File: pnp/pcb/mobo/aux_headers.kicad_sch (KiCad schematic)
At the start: 0 parts

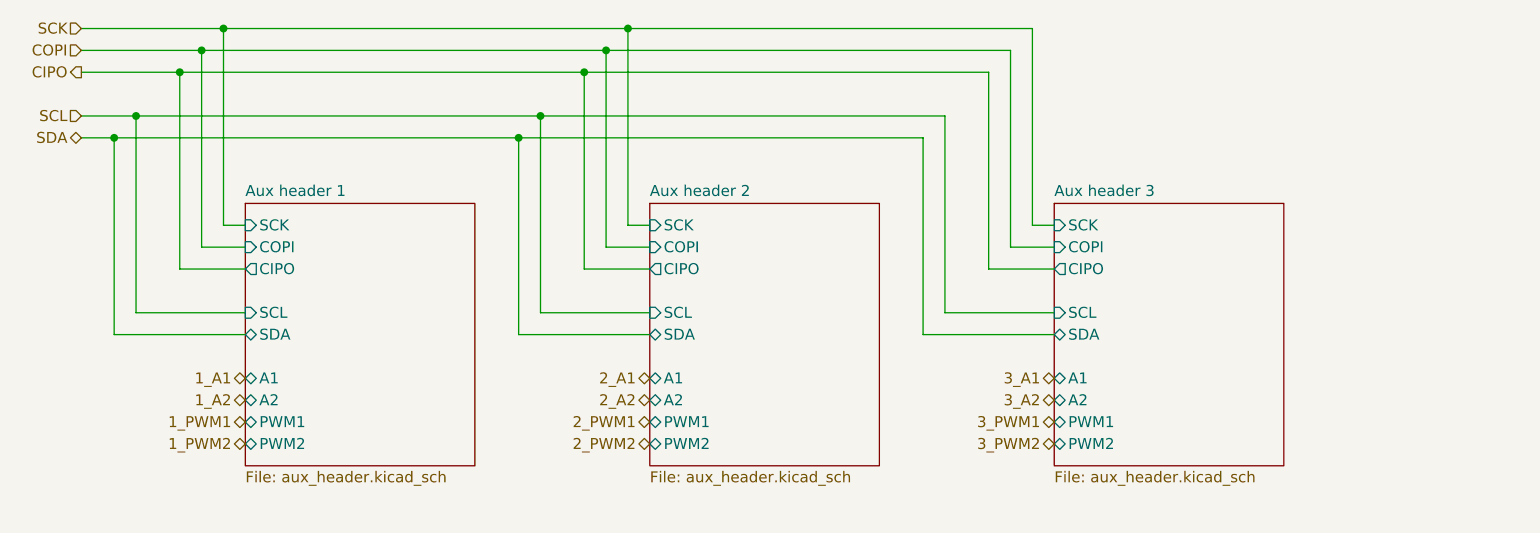
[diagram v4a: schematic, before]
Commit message: adds tons of TVS and inline resistors
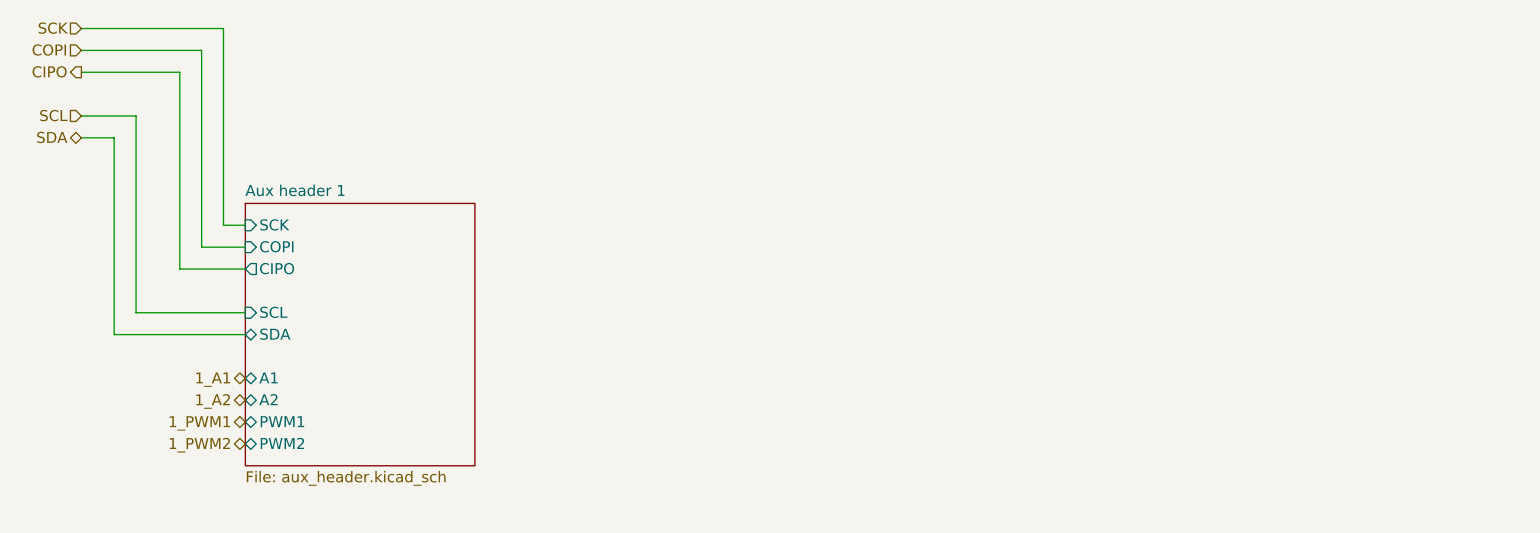
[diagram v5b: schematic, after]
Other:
- removed sheet Aux header 2
- removed sheet Aux header 3
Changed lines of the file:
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@@
     (company "Opulo")
-  )
-  (junction (at 85.09 73.66) (diameter 0) (color 0 0 0 0)
-  )
-  (junction (at 137.16 68.58) (diameter 0) (color 0 0 0 0)
-  )
-  (junction (at 77.47 81.28) (diameter 0) (color 0 0 0 0)
-  )
-  (junction (at 124.46 81.28) (diameter 0) (color 0 0 0 0)
-  )
-  (junction (at 80.01 78.74) (diameter 0) (color 0 0 0 0)
-  )
-  (junction (at 87.63 71.12) (diameter 0) (color 0 0 0 0)
-  )
-  (junction (at 132.08 73.66) (diameter 0) (color 0 0 0 0)
-  )
-  (junction (at 134.62 71.12) (diameter 0) (color 0 0 0 0)
-  )
-  (junction (at 127 78.74) (diameter 0) (color 0 0 0 0)
-  )
-  (junction (at 90.17 68.58) (diameter 0) (color 0 0 0 0)
   )
   (wire (pts (xy 90.17 91.44) (xy 90.17 68.58))
@@
     (stroke (width 0) (type default))
   )
-  (wire (pts (xy 134.62 71.12) (xy 181.61 71.12))
-    (stroke (width 0) (type default))
-  )
   (wire (pts (xy 90.17 91.44) (xy 92.71 91.44))
     (stroke (width 0) (type default))
@@
     (stroke (width 0) (type default))
   )
-  (wire (pts (xy 139.7 101.6) (xy 127 101.6))
-    (stroke (width 0) (type default))
-  )
-  (wire (pts (xy 171.45 104.14) (xy 186.69 104.14))
-    (stroke (width 0) (type default))
-  )
-  (wire (pts (xy 137.16 91.44) (xy 137.16 68.58))
-    (stroke (width 0) (type default))
-  )
-  (wire (pts (xy 127 78.74) (xy 173.99 78.74))
-    (stroke (width 0) (type default))
-  )
-  (wire (pts (xy 179.07 96.52) (xy 186.69 96.52))
-    (stroke (width 0) (type default))
-  )
-  (wire (pts (xy 124.46 81.28) (xy 124.46 104.14))
-    (stroke (width 0) (type default))
-  )
-  (wire (pts (xy 184.15 91.44) (xy 184.15 68.58))
-    (stroke (width 0) (type default))
-  )
-  (wire (pts (xy 181.61 93.98) (xy 186.69 93.98))
-    (stroke (width 0) (type default))
-  )
   (wire (pts (xy 87.63 71.12) (xy 73.66 71.12))
     (stroke (width 0) (type default))
   )
-  (wire (pts (xy 186.69 101.6) (xy 173.99 101.6))
-    (stroke (width 0) (type default))
-  )
-  (wire (pts (xy 173.99 101.6) (xy 173.99 78.74))
-    (stroke (width 0) (type default))
-  )
   (wire (pts (xy 85.09 96.52) (xy 92.71 96.52))
-    (stroke (width 0) (type default))
-  )
-  (wire (pts (xy 124.46 104.14) (xy 139.7 104.14))
-    (stroke (width 0) (type default))
-  )
-  (wire (pts (xy 132.08 96.52) (xy 132.08 73.66))
-    (stroke (width 0) (type default))
-  )
-  (wire (pts (xy 132.08 73.66) (xy 179.07 73.66))
     (stroke (width 0) (type default))
   )
@@
     (stroke (width 0) (type default))
   )
-  (wire (pts (xy 124.46 81.28) (xy 171.45 81.28))
-    (stroke (width 0) (type default))
-  )
   (wire (pts (xy 87.63 93.98) (xy 92.71 93.98))
     (stroke (width 0) (type default))
@@
     (stroke (width 0) (type default))
   )
-  (wire (pts (xy 184.15 91.44) (xy 186.69 91.44))
-    (stroke (width 0) (type default))
-  )
-  (wire (pts (xy 85.09 73.66) (xy 132.08 73.66))
-    (stroke (width 0) (type default))
-  )
-  (wire (pts (xy 134.62 93.98) (xy 139.7 93.98))
-    (stroke (width 0) (type default))
-  )
-  (wire (pts (xy 90.17 68.58) (xy 137.16 68.58))
-    (stroke (width 0) (type default))
-  )
-  (wire (pts (xy 137.16 68.58) (xy 184.15 68.58))
-    (stroke (width 0) (type default))
-  )
-  (wire (pts (xy 127 101.6) (xy 127 78.74))
-    (stroke (width 0) (type default))
-  )
-  (wire (pts (xy 171.45 81.28) (xy 171.45 104.14))
-    (stroke (width 0) (type default))
-  )
-  (wire (pts (xy 179.07 96.52) (xy 179.07 73.66))
-    (stroke (width 0) (type default))
-  )
-  (wire (pts (xy 80.01 78.74) (xy 127 78.74))
-    (stroke (width 0) (type default))
-  )
-  (wire (pts (xy 87.63 71.12) (xy 134.62 71.12))
-    (stroke (width 0) (type default))
-  )
   (wire (pts (xy 80.01 101.6) (xy 80.01 78.74))
-    (stroke (width 0) (type default))
-  )
-  (wire (pts (xy 134.62 93.98) (xy 134.62 71.12))
-    (stroke (width 0) (type default))
-  )
-  (wire (pts (xy 77.47 81.28) (xy 124.46 81.28))
     (stroke (width 0) (type default))
   )
@@
     (stroke (width 0) (type default))
   )
-  (wire (pts (xy 181.61 93.98) (xy 181.61 71.12))
-    (stroke (width 0) (type default))
-  )
-  (wire (pts (xy 137.16 91.44) (xy 139.7 91.44))
-    (stroke (width 0) (type default))
-  )
-  (wire (pts (xy 132.08 96.52) (xy 139.7 96.52))
-    (stroke (width 0) (type default))
-  )
-  (hierarchical_label "2_PWM1" (shape bidirectional) (at 139.7 114.3 180) (fields_autoplaced)
-    (effects (font (size 1.27 1.27)) (justify right))
-  )
   (hierarchical_label "SCL" (shape input) (at 73.66 78.74 180) (fields_autoplaced)
-    (effects (font (size 1.27 1.27)) (justify right))
-  )
-  (hierarchical_label "2_A2" (shape bidirectional) (at 139.7 111.76 180) (fields_autoplaced)
     (effects (font (size 1.27 1.27)) (justify right))
   )
@@
     (effects (font (size 1.27 1.27)) (justify right))
   )
-  (hierarchical_label "3_PWM2" (shape bidirectional) (at 186.69 116.84 180) (fields_autoplaced)
-    (effects (font (size 1.27 1.27)) (justify right))
-  )
   (hierarchical_label "1_PWM2" (shape bidirectional) (at 92.71 116.84 180) (fields_autoplaced)
-    (effects (font (size 1.27 1.27)) (justify right))
-  )
-  (hierarchical_label "3_PWM1" (shape bidirectional) (at 186.69 114.3 180) (fields_autoplaced)
     (effects (font (size 1.27 1.27)) (justify right))
   )
@@
   )
   (hierarchical_label "1_A1" (shape bidirectional) (at 92.71 109.22 180) (fields_autoplaced)
-    (effects (font (size 1.27 1.27)) (justify right))
-  )
-  (hierarchical_label "2_A1" (shape bidirectional) (at 139.7 109.22 180) (fields_autoplaced)
-    (effects (font (size 1.27 1.27)) (justify right))
-  )
-  (hierarchical_label "3_A2" (shape bidirectional) (at 186.69 111.76 180) (fields_autoplaced)
-    (effects (font (size 1.27 1.27)) (justify right))
-  )
-  (hierarchical_label "2_PWM2" (shape bidirectional) (at 139.7 116.84 180) (fields_autoplaced)
-    (effects (font (size 1.27 1.27)) (justify right))
-  )
-  (hierarchical_label "3_A1" (shape bidirectional) (at 186.69 109.22 180) (fields_autoplaced)
     (effects (font (size 1.27 1.27)) (justify right))
   )
@@
       )
     )
-  )
-  (sheet (at 186.69 88.9) (size 26.67 30.48) (fields_autoplaced)
-    (stroke (width 0.1524) (type solid))
-    (fill (color 0 0 0 0.0000))
-    (property "Sheetname" "Aux header 3" (at 186.69 88.1884 0)
-      (effects (font (size 1.27 1.27)) (justify left bottom))
-    )
-    (property "Sheetfile" "aux_header.kicad_sch" (at 186.69 119.9646 0)
-      (effects (font (size 1.27 1.27)) (justify left top))
-    )
-    (pin "PWM1" bidirectional (at 186.69 114.3 180)
-      (effects (font (size 1.27 1.27)) (justify left))
-    )
-    (pin "A2" bidirectional (at 186.69 111.76 180)
-      (effects (font (size 1.27 1.27)) (justify left))
-    )
-    (pin "A1" bidirectional (at 186.69 109.22 180)
-      (effects (font (size 1.27 1.27)) (justify left))
-    )
-    (pin "PWM2" bidirectional (at 186.69 116.84 180)
-      (effects (font (size 1.27 1.27)) (justify left))
-    )
-    (pin "COPI" input (at 186.69 93.98 180)
-      (effects (font (size 1.27 1.27)) (justify left))
-    )
-    (pin "CIPO" output (at 186.69 96.52 180)
-      (effects (font (size 1.27 1.27)) (justify left))
-    )
-    (pin "SCL" input (at 186.69 101.6 180)
-      (effects (font (size 1.27 1.27)) (justify left))
-    )
-    (pin "SCK" input (at 186.69 91.44 180)
-      (effects (font (size 1.27 1.27)) (justify left))
-    )
-    (pin "SDA" bidirectional (at 186.69 104.14 180)
-      (effects (font (size 1.27 1.27)) (justify left))
-    )
-    (instances
-      (project "mobo"
-        (path "/7255cbd1-8d38-4545-be9a-7fc5488ef942/00000000-0000-0000-0000-00005eb0c492" (page "27"))
-      )
-    )
-  )
-  (sheet (at 139.7 88.9) (size 26.67 30.48) (fields_autoplaced)
-    (stroke (width 0.1524) (type solid))
-    (fill (color 0 0 0 0.0000))
-    (property "Sheetname" "Aux header 2" (at 139.7 88.1884 0)
-      (effects (font (size 1.27 1.27)) (justify left bottom))
-    )
-    (property "Sheetfile" "aux_header.kicad_sch" (at 139.7 119.9646 0)
-      (effects (font (size 1.27 1.27)) (justify left top))
-    )
-    (pin "PWM1" bidirectional (at 139.7 114.3 180)
-      (effects (font (size 1.27 1.27)) (justify left))
-    )
-    (pin "A2" bidirectional (at 139.7 111.76 180)
-      (effects (font (size 1.27 1.27)) (justify left))
-    )
-    (pin "A1" bidirectional (at 139.7 109.22 180)
-      (effects (font (size 1.27 1.27)) (justify left))
-    )
-    (pin "PWM2" bidirectional (at 139.7 116.84 180)
-      (effects (font (size 1.27 1.27)) (justify left))
-    )
-    (pin "COPI" input (at 139.7 93.98 180)
-      (effects (font (size 1.27 1.27)) (justify left))
-    )
-    (pin "CIPO" output (at 139.7 96.52 180)
-      (effects (font (size 1.27 1.27)) (justify left))
-    )
-    (pin "SCL" input (at 139.7 101.6 180)
-      (effects (font (size 1.27 1.27)) (justify left))
-    )
-    (pin "SCK" input (at 139.7 91.44 180)
-      (effects (font (size 1.27 1.27)) (justify left))
-    )
-    (pin "SDA" bidirectional (at 139.7 104.14 180)
-      (effects (font (size 1.27 1.27)) (justify left))
-    )
-    (instances
-      (project "mobo"
-        (path "/7255cbd1-8d38-4545-be9a-7fc5488ef942/00000000-0000-0000-0000-00005eb0c492" (page "19"))
-      )
-    )
